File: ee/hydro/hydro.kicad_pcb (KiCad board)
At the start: 2 copper layers, 78 x 46 mm, 53 parts, among them J1 PJ-002A, J16 USB_B_Micro, J18 TC2030, J19 Conn_01x04_Male, J2 Conn_01x02_Male, J4 Conn_01x02_Male, J6 Conn_01x04_Male, J7 Conn_01x02_Male, Q1 DMP3099L-13, Q3 DMP3099L-13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

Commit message: Working on the board, parts are in place. Need som mounting holes.
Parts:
- removed J18: TC2030, Connector:Tag-Connect_TC2030-IDC-NL_2x03_P1.27mm_Vertical
- removed J19: Conn_01x04_Male, Connector_PinHeader_1.00mm:PinHeader_1x04_P1.00mm_Vertical
- added C21: 1uF, Capacitor_SMD:C_0805_2012Metric, F.Cu at (126.4, 154.9)
- added D3: MBR0540, Diode_SMD:D_SOD-123, F.Cu at (154.2, 165.7)
- added D4: MBR0540, Diode_SMD:D_SOD-123, F.Cu at (145.3, 165.7)
- added J8: Conn_02x10_Counter_Clockwise, Connector_PinHeader_2.54mm:PinHeader_2x10_P2.54mm_Vertical, F.Cu at (115.3, 136.3)
- J1: value PJ-002A -> PJ-036AH-SMT-TR
- SW1: value SW_Push_Dual -> SW_Push
- moved R5 86.6 mm to (145.3, 162.7), turned to 270 degrees
- moved R3 75.2 mm to (154.2, 162.7), turned to 270 degrees
- moved C9 72.1 mm to (111.6, 162.6), turned to 180 degrees
- moved Q1 67.7 mm to (151.4, 162.7), turned to 180 degrees
- moved R9 66.0 mm to (95.5, 172.6), turned to 90 degrees
- moved R19 65.0 mm to (112.8, 157.0), turned to 180 degrees
- moved R10 64.9 mm to (97.4, 172.6), turned to 90 degrees
- moved R1 63.1 mm to (130.2, 146.4)
- moved C15 62.8 mm to (125.6, 147.4)
- moved C13 62.6 mm to (125.6, 149.6)
- moved R2 62.4 mm to (130.2, 148.3), turned to 180 degrees
- moved Q3 61.1 mm to (142.5, 162.7), turned to 180 degrees
- moved D1 61.1 mm to (109.5, 157.0), turned to 180 degrees
- moved C11 60.7 mm to (103.5, 146.5), turned to 270 degrees
- moved C10 59.6 mm to (133.1, 151.9)
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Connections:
- net Net-(C10-Pad1) renamed /Power/SW
- net Net-(C10-Pad2) renamed /Power/VBST
- net Net-(C18-Pad1) renamed /Connector/LED_OUT
- net Net-(J7-Pad1) renamed /Connector/LED_FB
- net Net-(R1-Pad2) renamed /Power/VFB
- J1 pad 3: (no net) -> GND
- J2 pad 1: +12V -> Net-(D3-Pad2)
- J2 pad 2: Net-(J2-Pad2) -> +12V
- J4 pad 1: +12V -> Net-(D4-Pad2)
- J4 pad 2: Net-(J4-Pad2) -> +12V
- Q1 pad 1: Net-(J2-Pad2) -> Net-(D3-Pad2)
- Q3 pad 1: Net-(J4-Pad2) -> Net-(D4-Pad2)
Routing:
- net +3V3: track 29.2 -> 6.22 mm, vias 3 -> 0
- net /!RST: track 18.4 -> 5.87 mm, vias 2 -> 0
- net Net-(J19-Pad1): track 4.81 -> 0.00 mm
- net Net-(J19-Pad2): track 4.61 -> 0.00 mm
- net Net-(J19-Pad4): track 4.48 -> 0.00 mm
- net Net-(J19-Pad3): track 4.40 -> 0.00 mm
- net GND: track 2.69 -> 0.18 mm, vias 7 -> 0
- net LF_OSC_OUT: track 0.00 -> 2.33 mm, vias 0 -> 1
- net LF_OSC_IN: track 0.00 -> 2.13 mm, vias 0 -> 1
- net /TIM1_Pump1: track 1.78 -> 0.00 mm

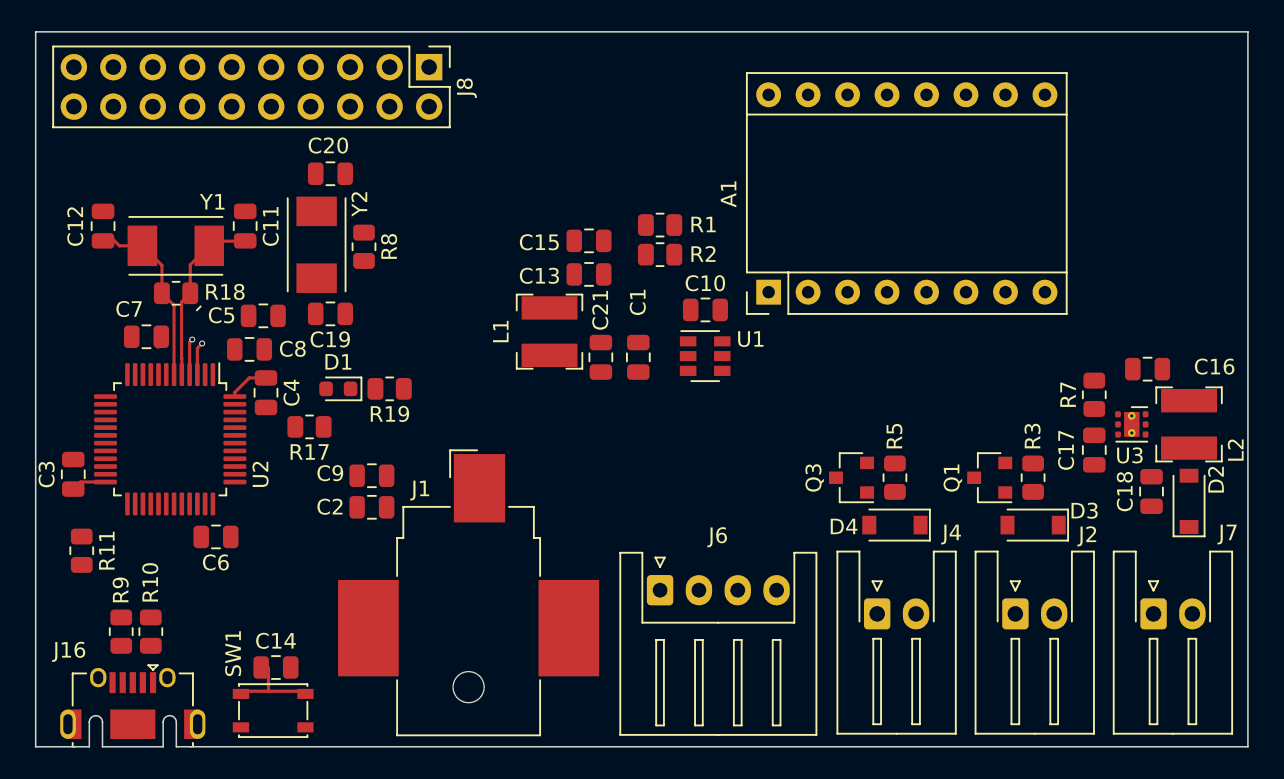
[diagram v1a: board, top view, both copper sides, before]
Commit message: Working on the ee parts of the design, placed two switches for fill and drain. Moved around some parts.
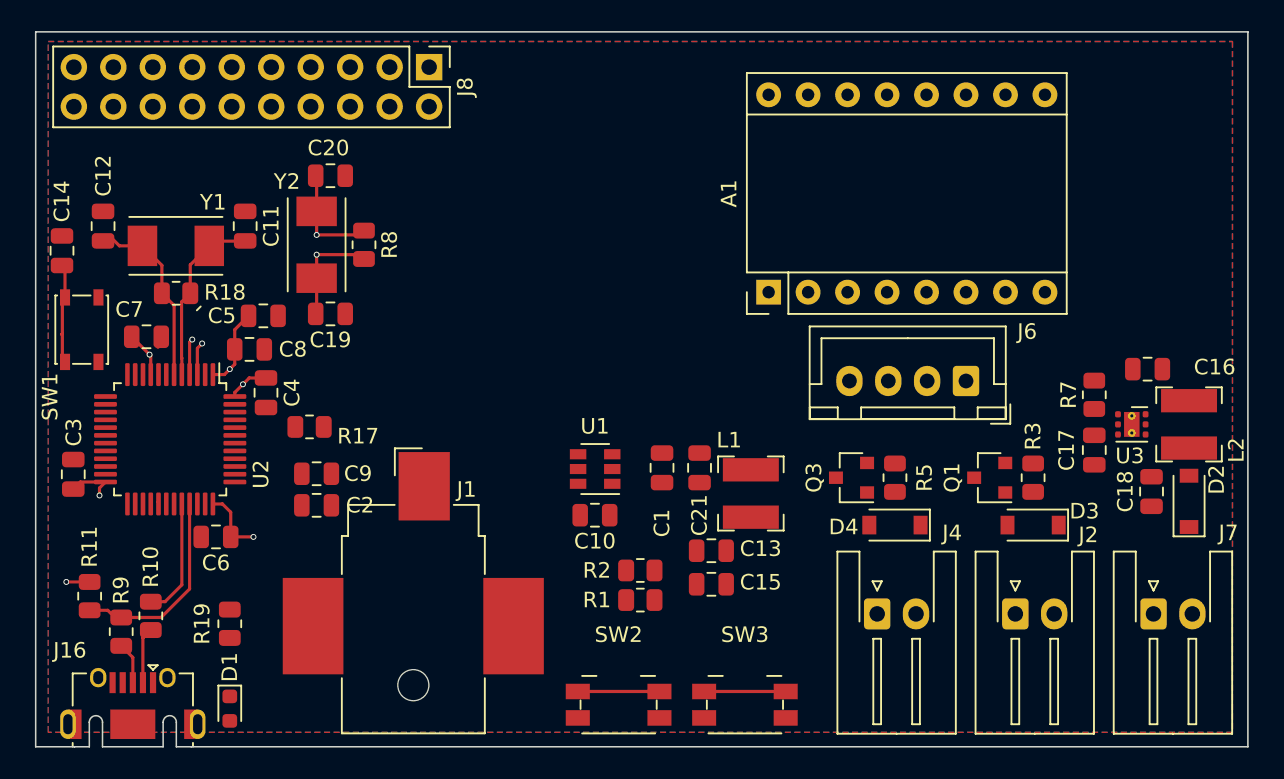
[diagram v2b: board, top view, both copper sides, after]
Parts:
- added SW2: Drain Tank, Button_Switch_SMD:Panasonic_EVQPUJ_EVQPUA, F.Cu at (127.5, 177.3)
- added SW3: Fill Tank, Button_Switch_SMD:Panasonic_EVQPUJ_EVQPUA, F.Cu at (135.6, 177.3)
- J6: footprint Connector_JST:JST_XH_S4B-XH-A_1x04_P2.50mm_Horizontal -> Connector_JST:JST_XH_B4B-XH-A_1x04_P2.50mm_Vertical
- SW1: value SW_Push -> Reset
- moved C14 30.1 mm to (91.7, 148.1), turned to 90 degrees
- moved SW1 27.4 mm to (93.0, 153.2), turned to 90 degrees
- moved R1 24.2 mm to (128.9, 170.6), turned to 180 degrees
- moved J6 23.8 mm to (149.9, 156.5), turned to 180 degrees
- moved C15 23.5 mm to (133.5, 169.5), turned to 180 degrees
- moved D1 21.7 mm to (102.5, 177.5), turned to 270 degrees
- moved R2 20.4 mm to (128.9, 168.7), turned to 0 degrees
- moved C13 19.4 mm to (133.5, 167.4), turned to 180 degrees
- moved R19 18.3 mm to (102.5, 172.1), turned to 270 degrees
- moved L1 16.6 mm to (136.0, 163.7), turned to 90 degrees
- moved C10 15.0 mm to (126.0, 165.1), turned to 180 degrees
- moved U1 10.1 mm to (126.0, 162.1), turned to 180 degrees
- moved C21 9.53 mm to (132.7, 162.1), turned to 270 degrees
- moved C1 7.27 mm to (130.3, 162.1), turned to 270 degrees
- moved C2 3.56 mm to (108.1, 164.5)
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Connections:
- J6 pad 3: Net-(A1-Pad3) -> Net-(A1-Pad4)
- J6 pad 4: Net-(A1-Pad4) -> Net-(A1-Pad3)
- J8 pad 13: /UART_RX -> Net-(J8-Pad13)
- J8 pad 14: /UART_TX -> Net-(J8-Pad14)
- J8 pad 15: /PA7 -> Net-(J8-Pad15)
- J8 pad 16: /PA6 -> Net-(J8-Pad16)
- J8 pad 17: /PA4 -> Net-(J8-Pad17)
- J8 pad 18: /PA3 -> Net-(J8-Pad18)
- J8 pad 19: /PA2 -> Net-(J8-Pad19)
- J8 pad 2: Net-(J8-Pad2) -> /SWDIO
- J8 pad 20: /PA1 -> Net-(J8-Pad20)
- J8 pad 3: Net-(J8-Pad3) -> /SWDCLK
- U2 pad 27: Net-(U2-Pad27) -> /Drain
- U2 pad 28: Net-(U2-Pad28) -> /Fill
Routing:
- net LF_OSC_OUT: track 2.33 -> 20.2 mm, vias 1 -> 2
- net LF_OSC_IN: track 2.13 -> 18.9 mm, vias 1 -> 2
- net +3V3: track 6.22 -> 21.3 mm, vias 0 -> 6
- net /USB_DP: track 0.00 -> 12.9 mm
- net /USB_DM: track 0.00 -> 7.65 mm
- net /Drain: track 0.00 -> 5.25 mm
- net /Fill: track 0.00 -> 5.25 mm
- net Net-(J16-Pad2): track 0.00 -> 3.60 mm
- net Net-(J16-Pad3): track 0.00 -> 2.68 mm
- net /!RST: track 5.87 -> 6.54 mm
- added copper zone on In1.Cu, net +3V3
- added copper zone on B.Cu, net GND
- added copper zone on F.Cu, net GND
- added copper zone on In2.Cu, net GND
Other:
- copper layers 2 -> 4

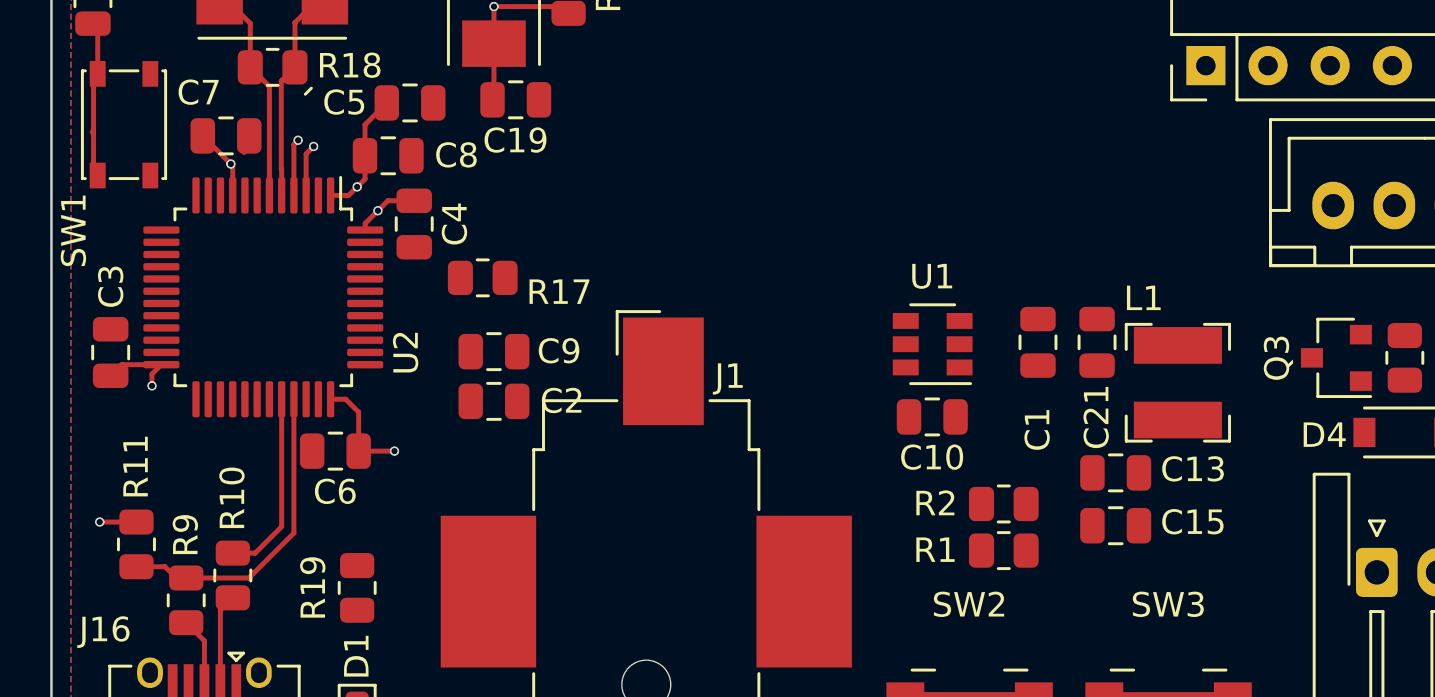
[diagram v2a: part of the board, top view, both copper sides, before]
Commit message: Routing out the pins for the MCU
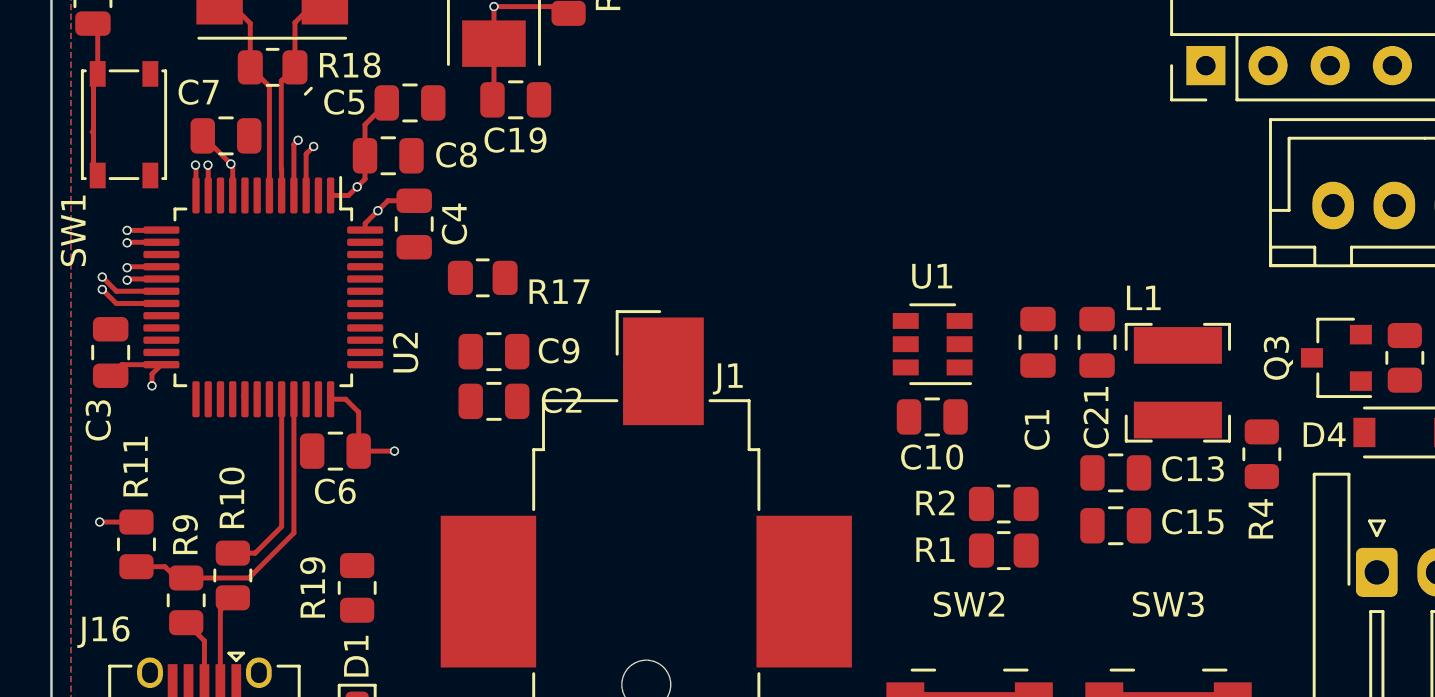
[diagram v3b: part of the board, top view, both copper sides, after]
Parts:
- added R4: 0R, Resistor_SMD:R_0805_2012Metric, F.Cu at (139.4, 166.6)
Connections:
- net Net-(U2-Pad18) renamed /PB0
- net Net-(U2-Pad19) renamed /PB1
- C13 pad 1: +3V3 -> Net-(C13-Pad1)
- C15 pad 1: +3V3 -> Net-(C13-Pad1)
- L1 pad 1: +3V3 -> Net-(C13-Pad1)
- R1 pad 1: +3V3 -> Net-(C13-Pad1)
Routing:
- net /PB1: track 0.00 -> 15.1 mm, vias 0 -> 1
- net /PB0: track 0.00 -> 14.3 mm, vias 0 -> 1
- net /PA7: track 0.00 -> 13.7 mm, vias 0 -> 1
- net /PA6: track 0.00 -> 12.9 mm, vias 0 -> 1
- net /PA4: track 0.00 -> 11.9 mm, vias 0 -> 1
- net /PA3: track 0.00 -> 11.0 mm, vias 0 -> 1
- net /PA2: track 0.00 -> 7.22 mm, vias 0 -> 1
- net /PA1: track 0.00 -> 7.21 mm, vias 0 -> 1

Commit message: Working on the board
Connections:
- D1 pad 2: /PC13 -> /LED
- J8 pad 13: Net-(J8-Pad13) -> /PA2
- J8 pad 14: Net-(J8-Pad14) -> /PA1
- J8 pad 15: Net-(J8-Pad15) -> /PA4
- J8 pad 16: Net-(J8-Pad16) -> /PA3
- J8 pad 17: Net-(J8-Pad17) -> /PA7
- J8 pad 18: Net-(J8-Pad18) -> /PA6
- J8 pad 19: Net-(J8-Pad19) -> /PB0
- J8 pad 20: Net-(J8-Pad20) -> /PB1
- U2 pad 26: Net-(U2-Pad26) -> /LED

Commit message: Routing "finished", building a master todo list now.
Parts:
- removed R17: 0R, Resistor_SMD:R_0805_2012Metric
- added C22: 100uF, Capacitor_SMD:CP_Elec_6.3x5.4, F.Cu at (162.8, 148.0)
- added C23: 1uF, Capacitor_SMD:C_0805_2012Metric, F.Cu at (116.7, 158.1)
- added D5: LED Red, LED_SMD:LED_0603_1608Metric, F.Cu at (139.8, 157.9)
- added JP1: SolderJumper_3_Bridged12, Jumper:SolderJumper-3_P1.3mm_Bridged12_RoundedPad1.0x1.5mm_NumberLabels, B.Cu at (147.3, 143.4)
- added JP2: SolderJumper_3_Bridged12, Jumper:SolderJumper-3_P1.3mm_Bridged12_RoundedPad1.0x1.5mm_NumberLabels, B.Cu at (149.9, 143.4)
- added JP3: SolderJumper_3_Bridged12, Jumper:SolderJumper-3_P1.3mm_Bridged12_RoundedPad1.0x1.5mm_NumberLabels, B.Cu at (152.4, 143.4)
- added JP4: Jumper_2_Open, Jumper:SolderJumper-2_P1.3mm_Open_RoundedPad1.0x1.5mm, F.Cu at (116.7, 155.7)
- added JP5: Jumper_2_Bridged, Jumper:SolderJumper-2_P1.3mm_Bridged2Bar_RoundedPad1.0x1.5mm, B.Cu at (99.6, 159.4)
- added R12: 1M, Resistor_SMD:R_0805_2012Metric, F.Cu at (117.5, 148.0)
- added R13: 1M, Resistor_SMD:R_0805_2012Metric, F.Cu at (117.5, 144.5)
- added R6: 1k, Resistor_SMD:R_0805_2012Metric, F.Cu at (139.8, 154.4)
- added U4: ESP-12E, RF_Module:ESP-12E, F.Cu at (127.8, 147.1)
- D1: value LED -> LED Green
- moved A1 2.67 mm to (139.8, 150.9)
- moved J6 2.67 mm to (152.5, 156.6)
- moved C4 1.00 mm to (105.5, 156.5), turned to 0 degrees
- moved C5 0.89 mm to (103.8, 152.3)
- moved C19 0.13 mm to (109.1, 152.1)
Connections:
- A1 pad 13: /Connector/Mot_nRST -> /PB7
- A1 pad 14: /Connector/Mot_nSLP -> /PB8
- A1 pad 16: /Mot_Dir -> /PB9
- A1 pad 2: /Connector/Mot_Flt -> /Mot_Dir
- J8 pad 10: Net-(J8-Pad10) -> GND
- J8 pad 11: GND -> /UART1_RX
- J8 pad 12: Net-(J8-Pad12) -> /UART1_TX
- J8 pad 4: Net-(J8-Pad4) -> /ESP_TX
- J8 pad 5: Net-(J8-Pad5) -> /ESP_RX
- J8 pad 6: Net-(J8-Pad6) -> /ESP_SCLK
- J8 pad 7: Net-(J8-Pad7) -> /ESP_MOSI
- J8 pad 8: Net-(J8-Pad8) -> /ESP_MISO
- J8 pad 9: Net-(J8-Pad9) -> /ESP_CS0
- U2 pad 30: /UART_TX -> /UART1_TX
- U2 pad 31: /UART_RX -> /UART1_RX
- U2 pad 43: Net-(U2-Pad43) -> /PB7
- U2 pad 45: Net-(U2-Pad45) -> /PB8
- U2 pad 46: Net-(U2-Pad46) -> /PB9
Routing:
- net +12V: track 0.00 -> 122.5 mm, vias 0 -> 4
- net /Mot_En: track 0.00 -> 70.2 mm, vias 0 -> 1
- net /TIM2_LED: track 0.03 -> 69.4 mm, vias 0 -> 2
- net /TIM1_Pump1: track 0.00 -> 63.1 mm, vias 0 -> 2
- net /PB7: track 0.00 -> 56.4 mm, vias 0 -> 1
- net /TIM3_Pump2: track 0.00 -> 53.5 mm, vias 0 -> 3
- net /Mot_Dir: track 0.00 -> 53.4 mm, vias 0 -> 2
- net /PB8: track 0.00 -> 53.3 mm, vias 0 -> 1
- net /TIM4_Step: track 0.00 -> 53.2 mm, vias 0 -> 2
- net /PB9: track 0.00 -> 48.3 mm, vias 0 -> 1
- net /Fill: track 5.25 -> 48.4 mm, vias 0 -> 2
- net /ESP_MOSI: track 0.00 -> 41.4 mm, vias 0 -> 1
- net /ESP_SCLK: track 0.00 -> 39.1 mm, vias 0 -> 1
- net /ESP_RX: track 0.00 -> 38.6 mm, vias 0 -> 1
- net /SWDCLK: track 0.00 -> 37.0 mm, vias 0 -> 1
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- added copper zone on F.Cu, net +12V
- added copper zone on F.Cu, net /Power/SW
- added copper zone on In1.Cu, net /Power/SW
- added copper zone on F.Cu, net Net-(C13-Pad1)
- added copper zone on F.Cu, net Net-(D2-Pad2)
